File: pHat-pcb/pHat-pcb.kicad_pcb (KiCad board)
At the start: 2 copper layers, 65 x 30 mm, 16 parts, among them J1 Conn_02x20_Odd_Even, J2 Conn_01x24_Male, J3 Conn_Active_High, J4 Conn_Bat, J5 Conn_I2C, J8 Conn_Active_Low, SW1 SW_Push, U1 TPS61023_Breakout, U2 74HCT74, U3 DS3231M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

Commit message: Rev 1: layout complete
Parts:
- J8: footprint Connector_PinHeader_2.54mm:PinHeader_1x03_P2.54mm_Horizontal -> Connector_PinHeader_2.54mm:PinHeader_1x03_P2.54mm_Vertical
- R1: footprint Resistor_THT:R_Axial_DIN0207_L6.3mm_D2.5mm_P7.62mm_Horizontal -> Resistor_SMD:R_1206_3216Metric_Pad1.30x1.75mm_HandSolder
- U2, U4: footprint Package_DIP:DIP-14_W7.62mm_Socket -> user:SO-14_3.9x8.65mm_P1.27mm_HandSolder
- U3: footprint Package_SO:SOIC-16W_7.5x10.3mm_P1.27mm -> user:SOIC-16W_7.5x10.3mm_P1.27mm_HandSolder
- moved J3 17.3 mm to (100.8, 76.3), turned to 90 degrees
- moved J8 16.8 mm to (95.6, 76.3)
- moved SW1 8.69 mm to (113.4, 61.7), turned to 270 degrees
- moved U2 5.67 mm to (92.9, 63.9), turned to 90 degrees
- moved U4 5.14 mm to (103.4, 63.9), turned to 90 degrees
- moved R1 5.00 mm to (86.8, 63.9)
- moved J5 2.30 mm to (72.0, 76.5)
- moved U3 0.50 mm to (75.8, 66.1)
- moved J4 0.22 mm to (59.0, 75.1)
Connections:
- J4 pad 3: Net-(J4-Pad3) -> GND
- J4 pad 4: Net-(J4-Pad4) -> /Vin
- J5 pad 1: Net-(J5-Pad1) -> /GPIO3(SCL1)
- J5 pad 2: Net-(J5-Pad2) -> /GPIO2(SDA1)
- J8 pad 1: GND -> /Vin
- J8 pad 2: /Vin -> GND
- U1 pad 1: Net-(J4-Pad4) -> /Vin
- U1 pad 2: Net-(J4-Pad3) -> GND
- U3 pad 15: Net-(J5-Pad2) -> /GPIO2(SDA1)
- U3 pad 16: Net-(J5-Pad1) -> /GPIO3(SCL1)
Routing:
- net /Vin: track 0.00 -> 96.1 mm
- net /1~PRE: track 0.00 -> 79.8 mm
- net /GPIO16: track 0.00 -> 53.7 mm
- net /En: track 0.00 -> 49.0 mm, vias 0 -> 1
- net /GPIO2(SDA1): track 9.19 -> 46.6 mm, vias 0 -> 1
- net /GPIO3(SCL1): track 9.61 -> 42.3 mm, vias 0 -> 1
- net +5V: track 2.54 -> 23.1 mm
- net /GPIO26: track 0.00 -> 20.1 mm, vias 0 -> 1
- net Net-(J3-Pad3): track 0.00 -> 16.9 mm
- net Net-(U2-Pad2): track 0.00 -> 10.9 mm
- net GND: track 10.4 -> 17.1 mm, vias 1 -> 3
- net +3V3: track 21.6 -> 23.2 mm
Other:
- net class +3,3V added: clearance 0.2, trace_width 0.4, via_dia 0.8, via_drill 0.4
- rule pad_to_mask_clearance: 0.051 -> 0
- board text added: "Battery"
- board text added: "En"
- board text added: "GND"
- board text added: "High->Low"
- board text added: "JLCJLCJLCJLC"
- board text added: "LBO"
- board text added: "Low->High"
- board text added: "Off"
- board text added: "On"
- board text added: "Rev 1"
- board text added: "Vin"
- board text added: "https://github.com/bablokb/pcb-pi-batman"

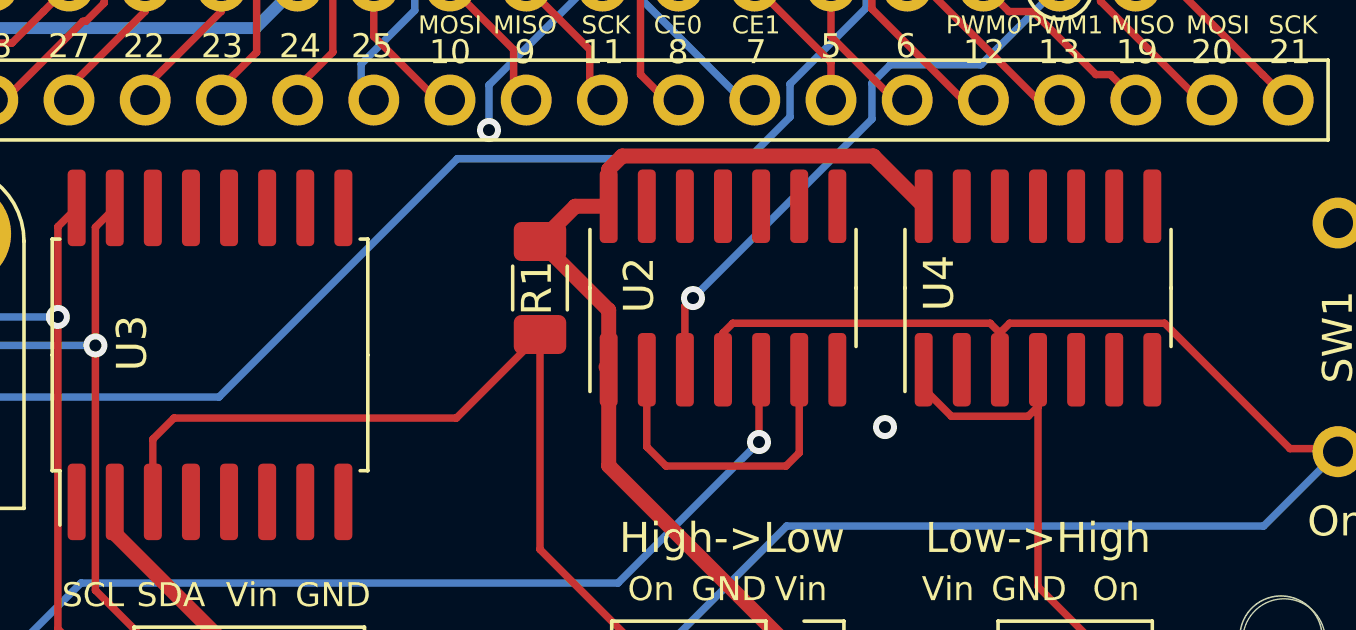
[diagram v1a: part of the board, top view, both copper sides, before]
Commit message: bugfix: replace 74HCT74 with 74HC74
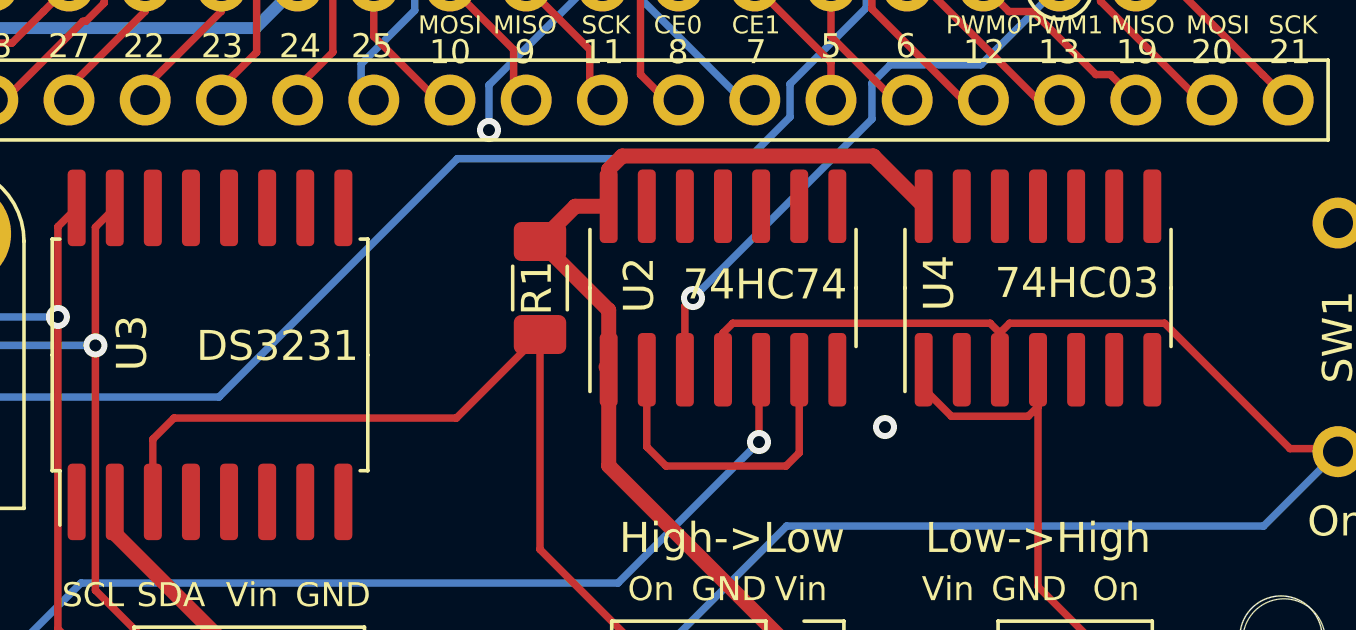
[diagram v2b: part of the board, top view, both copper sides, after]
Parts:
- U2: value 74HCT74 -> 74HC74
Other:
- board text added: "74HC03"
- board text added: "74HC74"
- board text added: "DS3231"

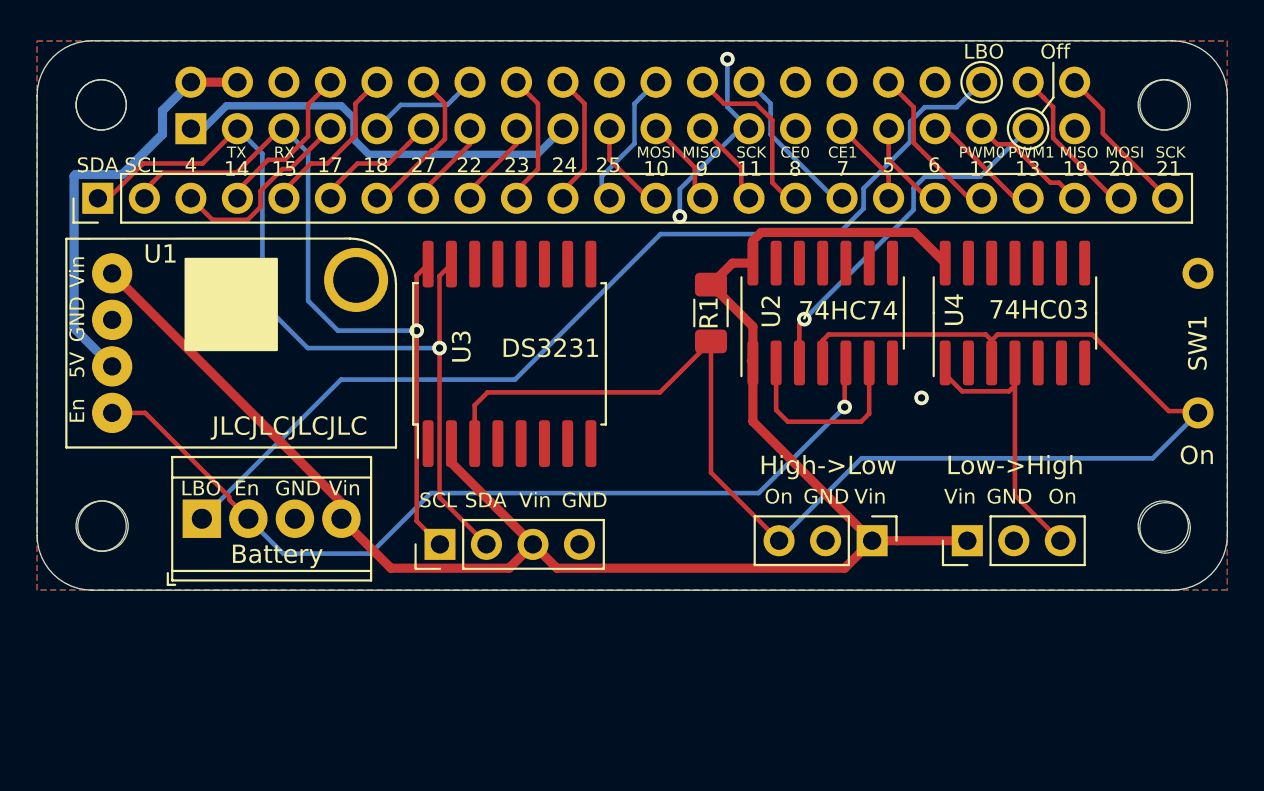
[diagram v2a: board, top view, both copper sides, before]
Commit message: Rev2: with DS3231 cap and no LBO-connector
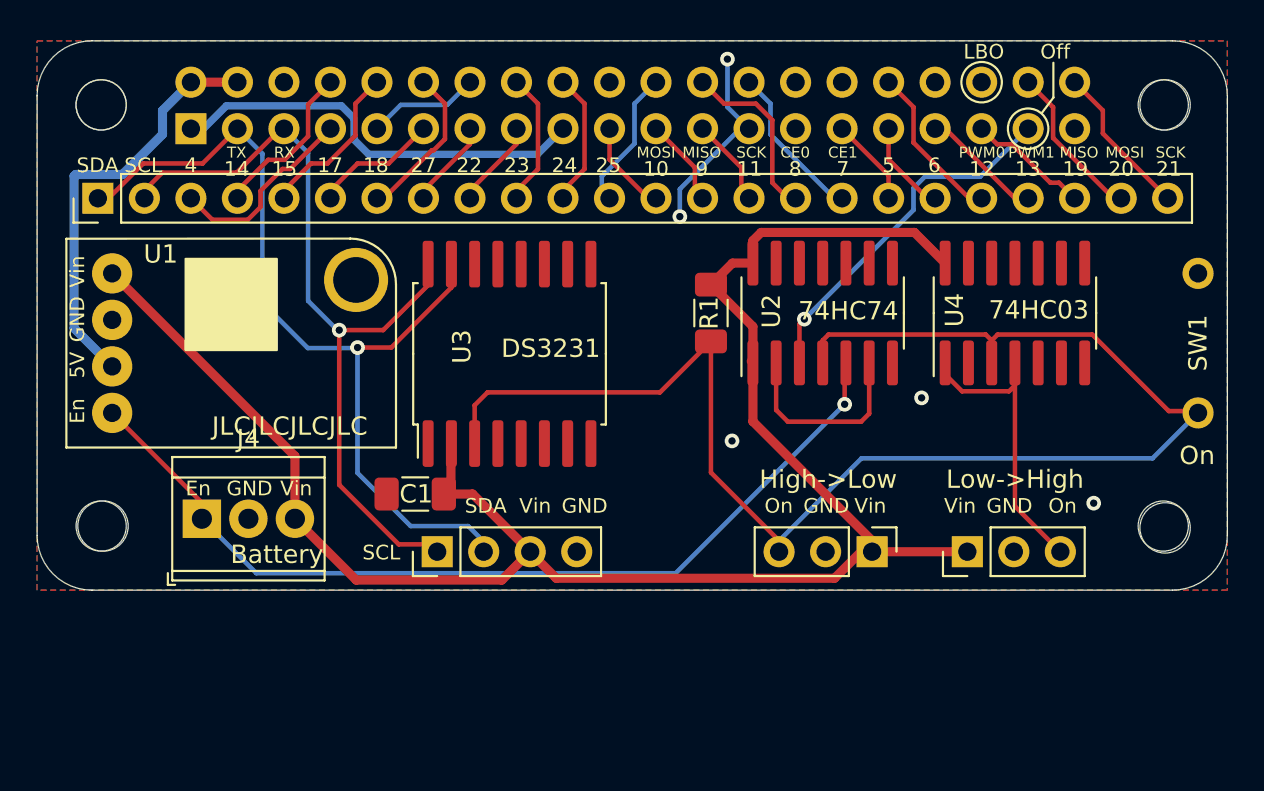
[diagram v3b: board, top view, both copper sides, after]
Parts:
- added C1: 100nF, Capacitor_SMD:C_1206_3216Metric_Pad1.33x1.80mm_HandSolder, F.Cu at (70.7, 73.8)
- J4: footprint TerminalBlock_TE-Connectivity:TerminalBlock_TE_282834-4_1x04_P2.54mm_Horizontal -> TerminalBlock_TE-Connectivity:TerminalBlock_TE_282834-3_1x03_P2.54mm_Horizontal
- moved J3 0.60 mm to (100.8, 76.9)
- moved J8 0.60 mm to (95.6, 76.9)
- moved J5 0.43 mm to (71.8, 76.9)
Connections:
- J4 pad 1: /GPIO16 -> /En
- J4 pad 2: /En -> GND
- J4 pad 3: GND -> /Vin
- U3 pad 14: Net-(U3-Pad14) -> GND
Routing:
- net /GPIO16: track 53.7 -> 0.00 mm
- net /Vin: track 96.1 -> 99.6 mm
- net /GPIO2(SDA1): track 46.6 -> 48.8 mm
- net /GPIO3(SCL1): track 42.3 -> 44.2 mm
- net /En: track 49.0 -> 50.3 mm
- net Net-(J3-Pad3): track 16.9 -> 17.5 mm
- net GND: vias 3 -> 5
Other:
- board text added: "Rev 2"
- board text removed: "Rev 1"

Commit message: Rev3: added power-control IC and LED
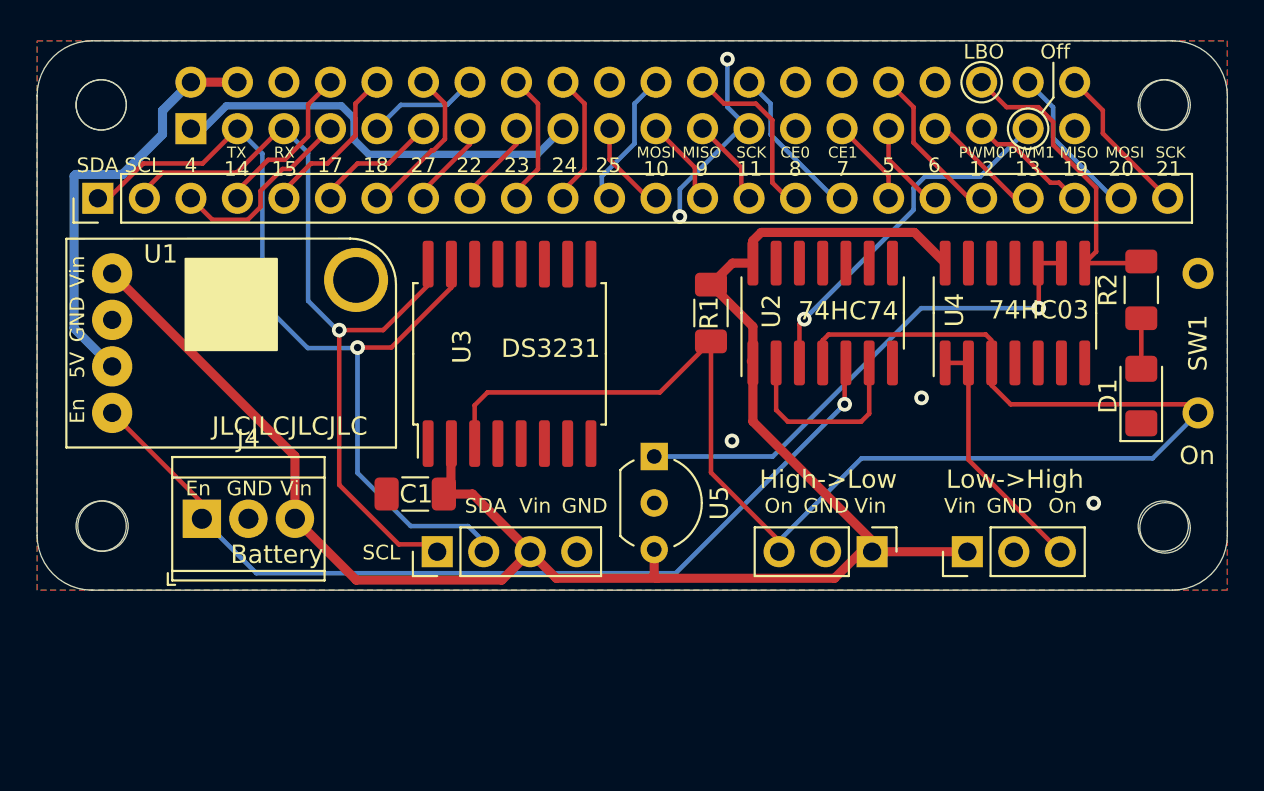
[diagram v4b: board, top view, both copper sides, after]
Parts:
- added D1: LED, LED_SMD:LED_1206_3216Metric_Pad1.42x1.75mm_HandSolder, F.Cu at (110.3, 68.4)
- added R2: 1kΩ, Resistor_SMD:R_1206_3216Metric_Pad1.30x1.75mm_HandSolder, F.Cu at (110.3, 62.6)
- added U5: KA75330, Package_TO_SOT_THT:TO-92_Inline_Wide, F.Cu at (83.7, 71.7)
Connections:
- U4 pad 10: Net-(U4-Pad10) -> /BatLow
- U4 pad 2: Net-(U4-Pad2) -> Net-(J3-Pad3)
- U4 pad 4: Net-(J3-Pad3) -> Net-(U4-Pad4)
- U4 pad 8: Net-(U4-Pad8) -> /GPIO16
- U4 pad 9: Net-(U4-Pad9) -> /BatLow
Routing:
- net /BatLow: track 0.00 -> 28.1 mm, vias 0 -> 1
- net /GPIO16: track 0.00 -> 16.9 mm
- net Net-(J3-Pad3): track 17.5 -> 14.3 mm
- net Net-(D1-Pad2): track 0.00 -> 3.00 mm
- net /Vin: track 99.6 -> 101.2 mm
- net /1~PRE: track 79.8 -> 78.5 mm
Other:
- board text added: "Rev 3"
- board text removed: "Rev 2"

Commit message: Rev4: added interrupt-pin for external I2C-connector
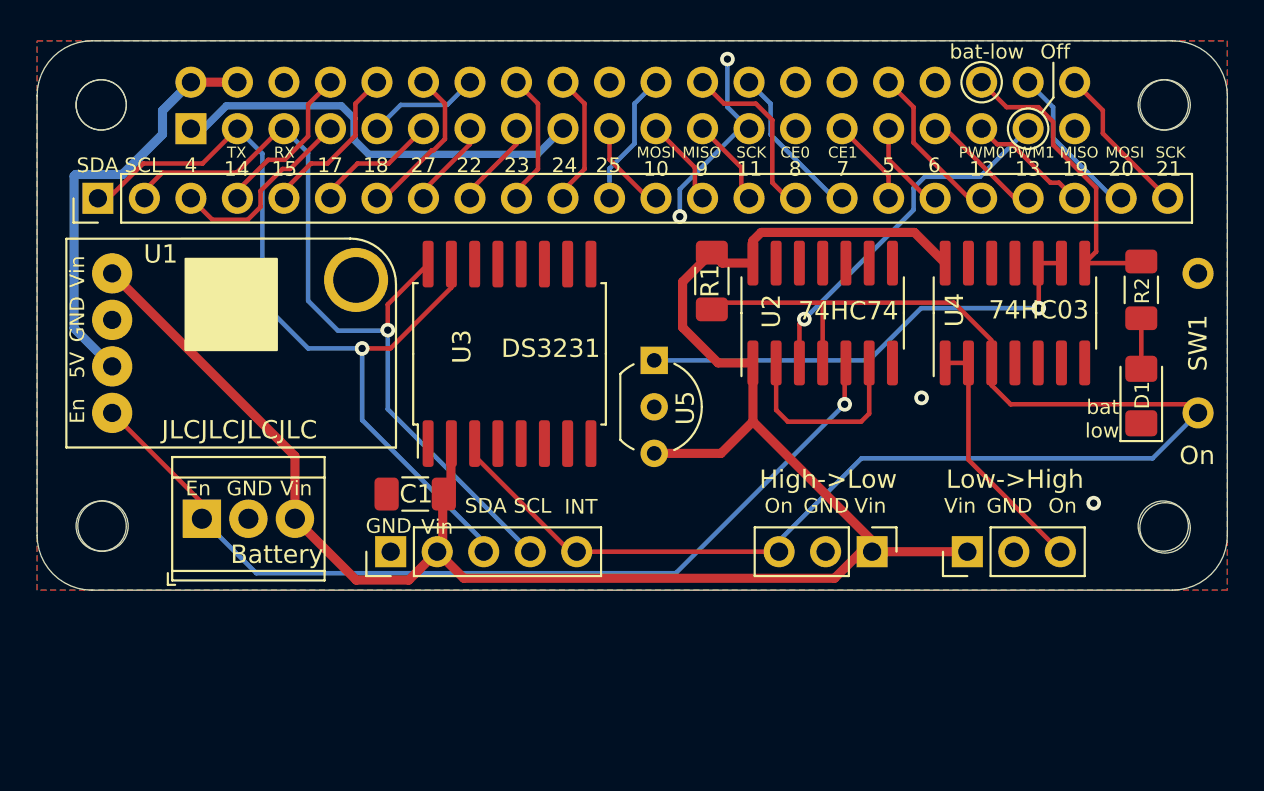
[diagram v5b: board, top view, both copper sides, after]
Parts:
- J5: footprint Connector_PinHeader_2.54mm:PinHeader_1x04_P2.54mm_Vertical -> Connector_PinHeader_2.54mm:PinHeader_1x05_P2.54mm_Vertical
- moved U5 5.25 mm to (83.7, 66.5)
- moved J5 2.54 mm to (69.3, 76.9)
- moved R1 1.75 mm to (86.8, 62.1)
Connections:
- J5 pad 1: /GPIO3(SCL1) -> GND
- J5 pad 2: /GPIO2(SDA1) -> /Vin
- J5 pad 3: /Vin -> /GPIO2(SDA1)
- J5 pad 4: GND -> /GPIO3(SCL1)
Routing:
- net /Vin: track 101.2 -> 107.1 mm
- net /BatLow: track 28.1 -> 25.9 mm
- net /GPIO2(SDA1): track 48.8 -> 46.8 mm
- net /1~PRE: track 78.5 -> 77.9 mm
- net GND: vias 5 -> 4
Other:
- board text added: "INT"
- board text added: "Rev 4"
- board text added: "bat low"
- board text added: "bat-low"
- board text removed: "LBO"
- board text removed: "Rev 3"

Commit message: Rev5: drive LED from GPIO06
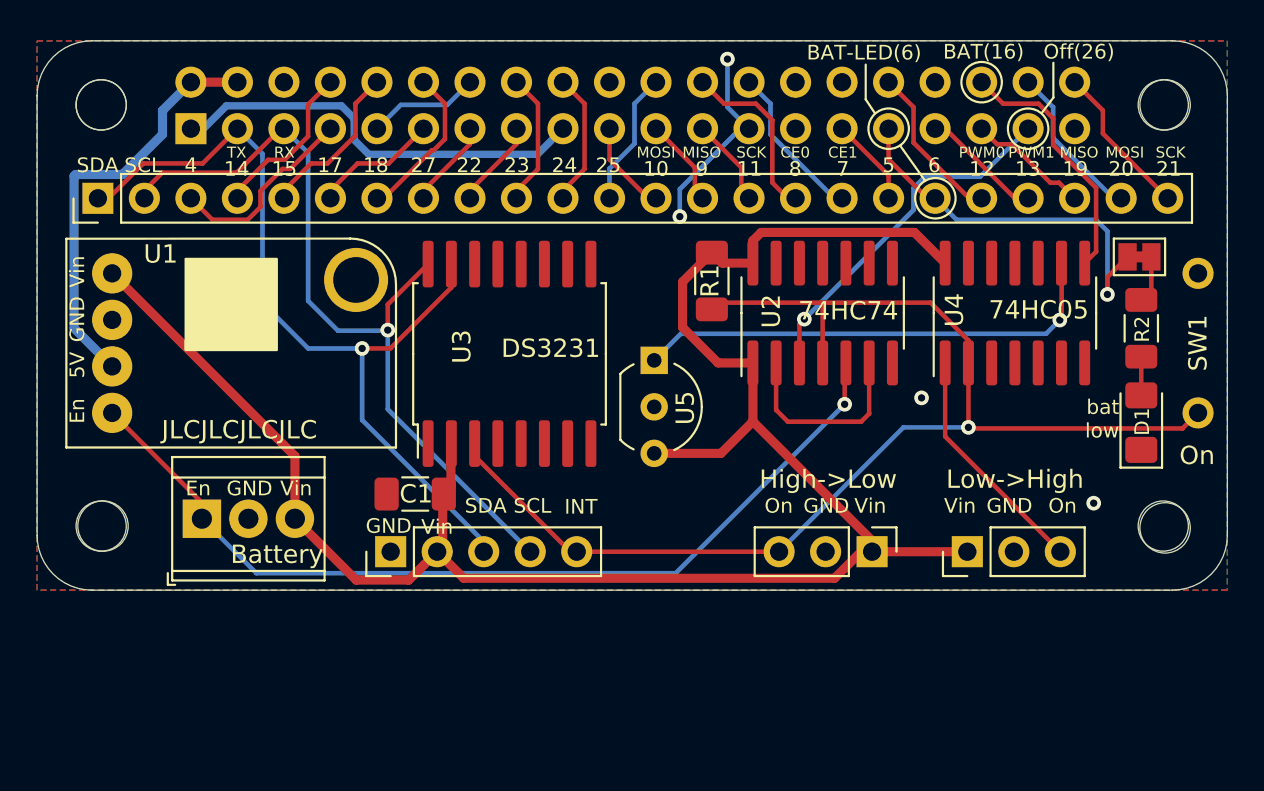
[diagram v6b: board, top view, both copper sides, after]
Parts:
- added JP1: SolderJumper_2_Bridged, Jumper:SolderJumper-2_P1.3mm_Bridged_Pad1.0x1.5mm, F.Cu at (110.2, 60.8)
- U4: value 74HC03 -> SN74HC05N
- moved R2 2.10 mm to (110.3, 64.7)
- moved D1 1.45 mm to (110.3, 69.8)
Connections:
- R2 pad 2: /GPIO16 -> Net-(JP1-Pad1)
- U4 pad 10: /BatLow -> Net-(U4-Pad10)
- U4 pad 11: Net-(U4-Pad11) -> GND
- U4 pad 13: Net-(U4-Pad13) -> GND
- U4 pad 2: Net-(J3-Pad3) -> /1~PRE
- U4 pad 3: /1~PRE -> GND
- U4 pad 5: Net-(U4-Pad5) -> GND
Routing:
- net /GPIO6: track 4.68 -> 20.8 mm, vias 0 -> 1
- net /1~PRE: track 77.9 -> 69.3 mm, vias 0 -> 1
- net /GPIO16: track 16.9 -> 13.9 mm
- net Net-(JP1-Pad1): track 0.00 -> 2.58 mm
- net Net-(D1-Pad2): track 3.00 -> 2.11 mm
- net Net-(J3-Pad3): track 14.3 -> 13.5 mm
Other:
- board text added: "74HC05"
- board text added: "BAT(16)"
- board text added: "BAT-LED(6)"
- board text added: "Off(26)"
- board text added: "Rev 5"
- board text removed: "74HC03"
- board text removed: "Off"
- board text removed: "Rev 4"
- board text removed: "bat-low"
